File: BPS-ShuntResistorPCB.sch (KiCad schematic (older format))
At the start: 3 parts, among them J1 Conn_01x04

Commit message: fixed labels
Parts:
- J1: value Conn_01x04 -> Amp_Conn
- R1: value R -> 100u
- TH1: value Thermistor -> 100
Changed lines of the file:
@@
 P 6850 4350
 F 0 "J1" H 6950 4400 50  0000 L CNN
-F 1 "Conn_01x04" H 6950 4300 50  0000 L CNN
+F 1 "Amp_Conn" H 6950 4300 50  0000 L CNN
 F 2 "" H 6850 4350 50  0001 C CNN
 F 3 "~" H 6850 4350 50  0001 C CNN
@@
 P 5950 4150
 F 0 "R1" H 6020 4196 50  0000 L CNN
-F 1 "R" H 6020 4105 50  0000 L CNN
+F 1 "100u" H 6020 4105 50  0000 L CNN
 F 2 "Resistor_SMD:R_0805_2012Metric" V 5880 4150 50  0001 C CNN
 F 3 "~" H 5950 4150 50  0001 C CNN
@@
 P 5950 4650
 F 0 "TH1" H 6055 4696 50  0000 L CNN
-F 1 "Thermistor" H 6055 4605 50  0000 L CNN
+F 1 "100" H 6055 4605 50  0000 L CNN
 F 2 "Resistor_SMD:R_0805_2012Metric" H 5950 4650 50  0001 C CNN
 F 3 "~" H 5950 4650 50  0001 C CNN

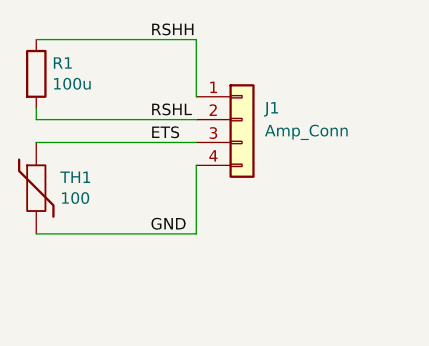
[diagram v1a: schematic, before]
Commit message: added logos and conn footprint
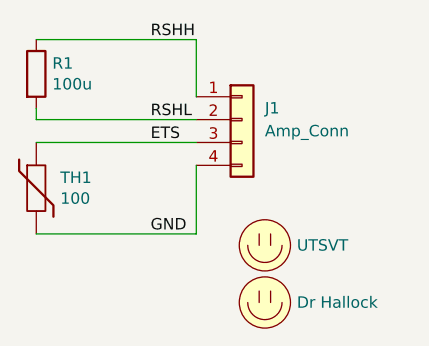
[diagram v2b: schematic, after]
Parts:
- added LOGO1: UTSVT, UTSVT_Special:UTSVT_Logo_Symbol, symbol utsvt-misc:Logo_Placeholder
- added LOGO2: Dr Hallock, UTSVT_Special:Hallock_Image_Tiny, symbol utsvt-misc:Logo_Placeholder
- J1: footprint (none) -> UTSVT_Connectors:Power_Metal_Strip_Battery_Shunt_Resistor_4_Pin_Connector
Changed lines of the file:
@@
 F 0 "J1" H 6950 4400 50  0000 L CNN
 F 1 "Amp_Conn" H 6950 4300 50  0000 L CNN
-F 2 "" H 6850 4350 50  0001 C CNN
+F 2 "UTSVT_Connectors:Power_Metal_Strip_Battery_Shunt_Resistor_4_Pin_Connector" H 6850 4350 50  0001 C CNN
 F 3 "~" H 6850 4350 50  0001 C CNN
 	1    6850 4350
@@
 	1    0    0    -1
 $EndComp
+$Comp
+L utsvt-misc:Logo_Placeholder LOGO1
+U 1 1 5F53FE42
+P 6950 4900
+F 0 "LOGO1" H 6950 5050 50  0001 C CNN
+F 1 "UTSVT" H 7090 4900 50  0000 L CNN
+F 2 "UTSVT_Special:UTSVT_Logo_Symbol" H 6950 4975 50  0001 C CNN
+F 3 "" H 6950 4975 50  0001 C CNN
+	1    6950 4900
+	1    0    0    -1
+$EndComp
+$Comp
+L utsvt-misc:Logo_Placeholder LOGO2
+U 1 1 5F5407D9
+P 6950 5150
+F 0 "LOGO2" H 6950 5300 50  0001 C CNN
+F 1 "Dr Hallock" H 7090 5150 50  0000 L CNN
+F 2 "UTSVT_Special:Hallock_Image_Tiny" H 6950 5225 50  0001 C CNN
+F 3 "" H 6950 5225 50  0001 C CNN
+	1    6950 5150
+	1    0    0    -1
+$EndComp

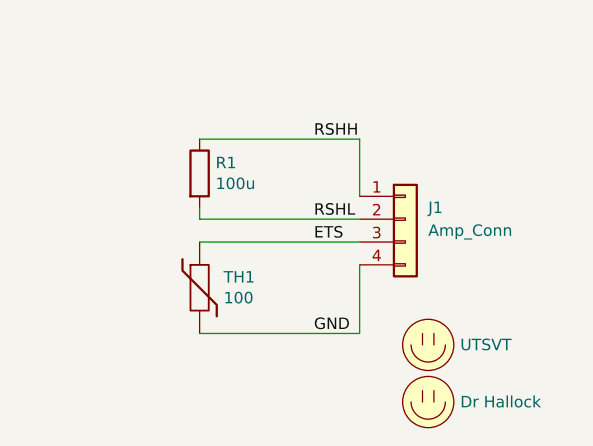
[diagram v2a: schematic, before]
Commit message: updated connector to match ampere board
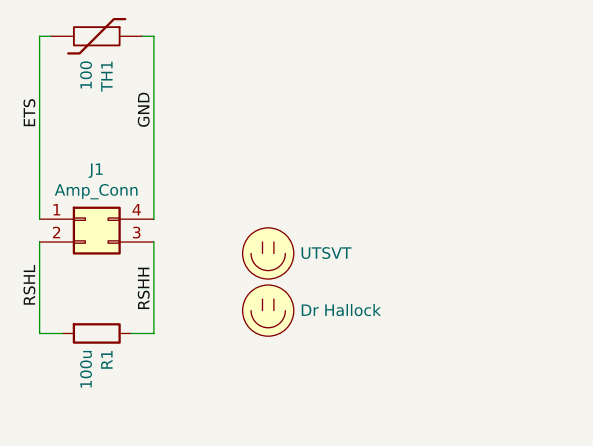
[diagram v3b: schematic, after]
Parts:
- removed J1: Amp_Conn, UTSVT_Connectors:Power_Metal_Strip_Battery_Shunt_Resistor_4_Pin_Connector, symbol Connector_Generic:Conn_01x04
- added J1: Amp_Conn, UTSVT_Connectors:Power_Metal_Strip_Battery_Shunt_Resistor_4_Pin_Connector, symbol Connector_Generic:Conn_02x02_Counter_Clockwise
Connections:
- net ETS: now also TH1.2, J1.1 (Pin_1); no longer TH1.1
- net GND: now also TH1.1, J1.4 (Pin_4); no longer TH1.2
- net RSHH: now also J1.3 (Pin_3)
- net RSHL: now also J1.2 (Pin_2)
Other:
- moved on the sheet: R1, TH1
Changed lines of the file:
@@
 Comment4 ""
 $EndDescr
-Wire Wire Line
-	6650 4250 6650 4000
-Wire Wire Line
-	6650 4000 5950 4000
-Wire Wire Line
-	5950 4300 5950 4350
-Wire Wire Line
-	5950 4350 6650 4350
-Wire Wire Line
-	6650 4550 6650 4850
-Wire Wire Line
-	6650 4850 5950 4850
-Wire Wire Line
-	5950 4450 6650 4450
-Text Label 6450 4000 0    50   ~ 0
+Text Label 5750 4750 1    50   ~ 0
 RSHH
-Text Label 6450 4350 0    50   ~ 0
+Text Label 5250 4550 3    50   ~ 0
 RSHL
-Text Label 6450 4450 0    50   ~ 0
+Text Label 5250 3950 1    50   ~ 0
 ETS
-Text Label 6450 4850 0    50   ~ 0
+Text Label 5750 3950 1    50   ~ 0
 GND
 $Comp
-L Connector_Generic:Conn_01x04 J1
-U 1 1 5F54708B
-P 6850 4350
-F 0 "J1" H 6950 4400 50  0000 L CNN
-F 1 "Amp_Conn" H 6950 4300 50  0000 L CNN
-F 2 "UTSVT_Connectors:Power_Metal_Strip_Battery_Shunt_Resistor_4_Pin_Connector" H 6850 4350 50  0001 C CNN
-F 3 "~" H 6850 4350 50  0001 C CNN
-	1    6850 4350
+L Device:Thermistor TH1
+U 1 1 5F548CAA
+P 5500 3550
+F 0 "TH1" H 5605 3596 50  0000 L CNN
+F 1 "100" H 5605 3505 50  0000 L CNN
+F 2 "Resistor_SMD:R_0805_2012Metric" H 5500 3550 50  0001 C CNN
+F 3 "~" H 5500 3550 50  0001 C CNN
+	1    5500 3550
+	0    1    1    0
+$EndComp
+$Comp
+L utsvt-misc:Logo_Placeholder LOGO1
+U 1 1 5F53FE42
+P 6250 4500
+F 0 "LOGO1" H 6250 4650 50  0001 C CNN
+F 1 "UTSVT" H 6390 4500 50  0000 L CNN
+F 2 "UTSVT_Special:UTSVT_Logo_Symbol" H 6250 4575 50  0001 C CNN
+F 3 "" H 6250 4575 50  0001 C CNN
+	1    6250 4500
+	1    0    0    -1
+$EndComp
+$Comp
+L utsvt-misc:Logo_Placeholder LOGO2
+U 1 1 5F5407D9
+P 6250 4750
+F 0 "LOGO2" H 6250 4900 50  0001 C CNN
+F 1 "Dr Hallock" H 6390 4750 50  0000 L CNN
+F 2 "UTSVT_Special:Hallock_Image_Tiny" H 6250 4825 50  0001 C CNN
+F 3 "" H 6250 4825 50  0001 C CNN
+	1    6250 4750
 	1    0    0    -1
 $EndComp
@@
 L Device:R R1
 U 1 1 5F548200
-P 5950 4150
-F 0 "R1" H 6020 4196 50  0000 L CNN
-F 1 "100u" H 6020 4105 50  0000 L CNN
-F 2 "Resistor_SMD:R_0805_2012Metric" V 5880 4150 50  0001 C CNN
-F 3 "~" H 5950 4150 50  0001 C CNN
-	1    5950 4150
+P 5500 4850
+F 0 "R1" H 5570 4896 50  0000 L CNN
+F 1 "100u" H 5570 4805 50  0000 L CNN
+F 2 "Resistor_SMD:R_0805_2012Metric" V 5430 4850 50  0001 C CNN
+F 3 "~" H 5500 4850 50  0001 C CNN
+	1    5500 4850
+	0    1    1    0
+$EndComp
+$Comp
+L Connector_Generic:Conn_02x02_Counter_Clockwise J1
+U 1 1 5F55AEC1
+P 5450 4350
+F 0 "J1" H 5500 4567 50  0000 C CNN
+F 1 "Amp_Conn" H 5500 4476 50  0000 C CNN
+F 2 "UTSVT_Connectors:Power_Metal_Strip_Battery_Shunt_Resistor_4_Pin_Connector" H 5450 4350 50  0001 C CNN
+F 3 "~" H 5450 4350 50  0001 C CNN
+	1    5450 4350
 	1    0    0    -1
 $EndComp
-$Comp
-L Device:Thermistor TH1
-U 1 1 5F548CAA
-P 5950 4650
-F 0 "TH1" H 6055 4696 50  0000 L CNN
-F 1 "100" H 6055 4605 50  0000 L CNN
-F 2 "Resistor_SMD:R_0805_2012Metric" H 5950 4650 50  0001 C CNN
-F 3 "~" H 5950 4650 50  0001 C CNN
-	1    5950 4650
-	1    0    0    -1
-$EndComp
-$Comp
-L utsvt-misc:Logo_Placeholder LOGO1
-U 1 1 5F53FE42
-P 6950 4900
-F 0 "LOGO1" H 6950 5050 50  0001 C CNN
-F 1 "UTSVT" H 7090 4900 50  0000 L CNN
-F 2 "UTSVT_Special:UTSVT_Logo_Symbol" H 6950 4975 50  0001 C CNN
-F 3 "" H 6950 4975 50  0001 C CNN
-	1    6950 4900
-	1    0    0    -1
-$EndComp
-$Comp
-L utsvt-misc:Logo_Placeholder LOGO2
-U 1 1 5F5407D9
-P 6950 5150
-F 0 "LOGO2" H 6950 5300 50  0001 C CNN
-F 1 "Dr Hallock" H 7090 5150 50  0000 L CNN
-F 2 "UTSVT_Special:Hallock_Image_Tiny" H 6950 5225 50  0001 C CNN
-F 3 "" H 6950 5225 50  0001 C CNN
-	1    6950 5150
-	1    0    0    -1
-$EndComp
+Wire Wire Line
+	5250 4350 5250 3550
+Wire Wire Line
+	5250 3550 5300 3550
+Wire Wire Line
+	5750 4350 5750 3550
+Wire Wire Line
+	5750 3550 5700 3550
+Wire Wire Line
+	5250 4450 5250 4850
+Wire Wire Line
+	5250 4850 5350 4850
+Wire Wire Line
+	5650 4850 5750 4850
+Wire Wire Line
+	5750 4850 5750 4450
 $EndSCHEMATC

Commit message: added resistor footprint
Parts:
- R1: footprint Resistor_SMD:R_0805_2012Metric -> UTSVT_Passive:Power_Metal_Strip_Battery_Shunt_Resistor
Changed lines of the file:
@@
 F 0 "R1" H 5570 4896 50  0000 L CNN
 F 1 "100u" H 5570 4805 50  0000 L CNN
-F 2 "Resistor_SMD:R_0805_2012Metric" V 5430 4850 50  0001 C CNN
+F 2 "UTSVT_Passive:Power_Metal_Strip_Battery_Shunt_Resistor" V 5430 4850 50  0001 C CNN
 F 3 "~" H 5500 4850 50  0001 C CNN
 	1    5500 4850

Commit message: needs to be reviewed
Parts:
- added H1, H2: MountingHole, MountingHole:MountingHole_2.7mm_M2.5, symbol Mechanical:MountingHole
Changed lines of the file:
@@
 Wire Wire Line
 	5750 4850 5750 4450
+$Comp
+L Mechanical:MountingHole H1
+U 1 1 5F6F5E19
+P 3000 2100
+F 0 "H1" H 3100 2146 50  0000 L CNN
+F 1 "MountingHole" H 3100 2055 50  0000 L CNN
+F 2 "MountingHole:MountingHole_2.7mm_M2.5" H 3000 2100 50  0001 C CNN
+F 3 "~" H 3000 2100 50  0001 C CNN
+	1    3000 2100
+	1    0    0    -1
+$EndComp
+$Comp
+L Mechanical:MountingHole H2
+U 1 1 5F6F8A03
+P 2950 2900
+F 0 "H2" H 3050 2946 50  0000 L CNN
+F 1 "MountingHole" H 3050 2855 50  0000 L CNN
+F 2 "MountingHole:MountingHole_2.7mm_M2.5" H 2950 2900 50  0001 C CNN
+F 3 "~" H 2950 2900 50  0001 C CNN
+	1    2950 2900
+	1    0    0    -1
+$EndComp
 $EndSCHEMATC

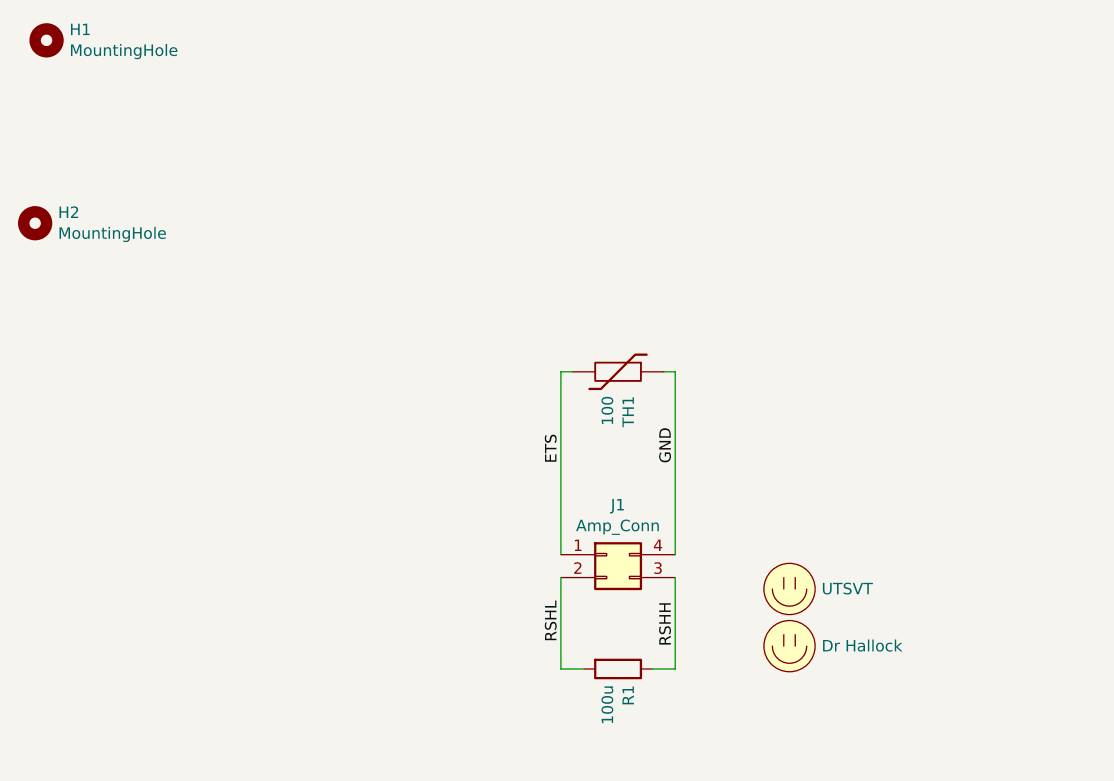
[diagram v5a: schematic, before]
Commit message: Organizes schematic and creates pdf and png files of schematic and PCB
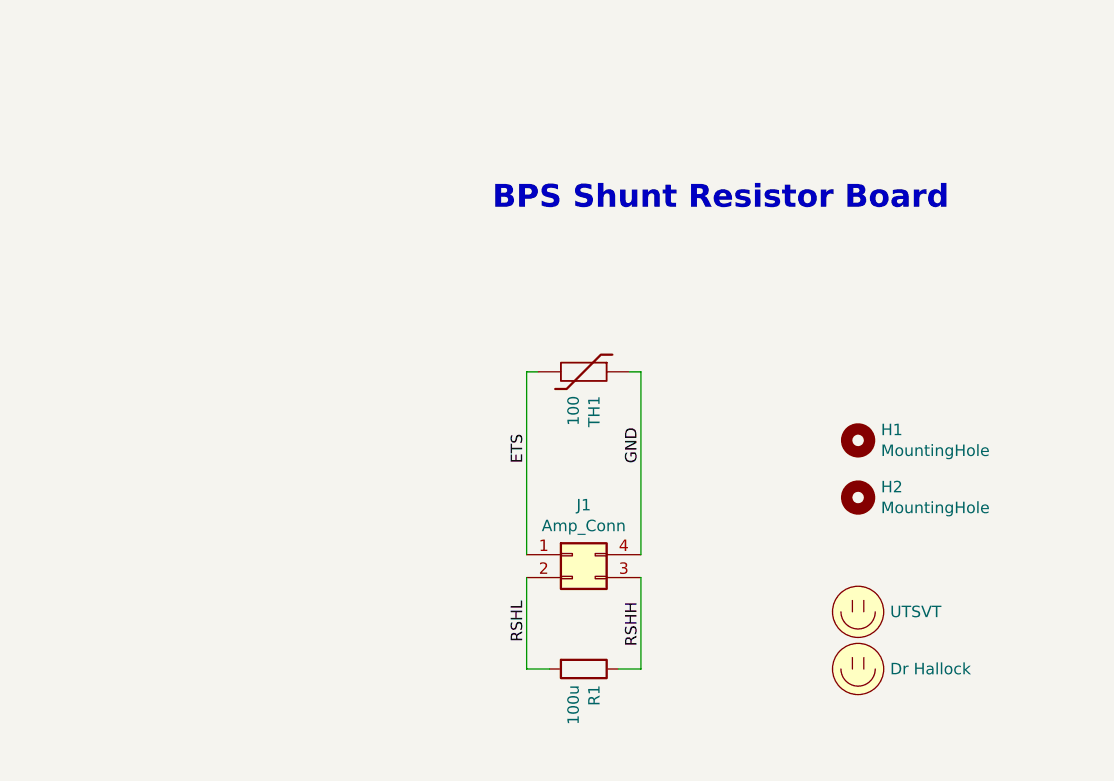
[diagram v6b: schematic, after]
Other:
- note added: "BPS Shunt Resistor Board"
- moved on the sheet: H1, H2, J1, R1, TH1
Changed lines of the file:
@@
 Comment4 ""
 $EndDescr
-Text Label 5750 4750 1    50   ~ 0
+Text Label 5600 4750 1    50   ~ 0
 RSHH
-Text Label 5250 4550 3    50   ~ 0
+Text Label 5100 4550 3    50   ~ 0
 RSHL
-Text Label 5250 3950 1    50   ~ 0
+Text Label 5100 3950 1    50   ~ 0
 ETS
-Text Label 5750 3950 1    50   ~ 0
+Text Label 5600 3950 1    50   ~ 0
 GND
 $Comp
 L Device:Thermistor TH1
 U 1 1 5F548CAA
-P 5500 3550
-F 0 "TH1" H 5605 3596 50  0000 L CNN
-F 1 "100" H 5605 3505 50  0000 L CNN
-F 2 "Resistor_SMD:R_0805_2012Metric" H 5500 3550 50  0001 C CNN
-F 3 "~" H 5500 3550 50  0001 C CNN
-	1    5500 3550
+P 5350 3550
+F 0 "TH1" H 5455 3596 50  0000 L CNN
+F 1 "100" H 5455 3505 50  0000 L CNN
+F 2 "Resistor_SMD:R_0805_2012Metric" H 5350 3550 50  0001 C CNN
+F 3 "~" H 5350 3550 50  0001 C CNN
+	1    5350 3550
 	0    1    1    0
 $EndComp
@@
 L utsvt-misc:Logo_Placeholder LOGO1
 U 1 1 5F53FE42
-P 6250 4500
-F 0 "LOGO1" H 6250 4650 50  0001 C CNN
-F 1 "UTSVT" H 6390 4500 50  0000 L CNN
-F 2 "UTSVT_Special:UTSVT_Logo_Symbol" H 6250 4575 50  0001 C CNN
-F 3 "" H 6250 4575 50  0001 C CNN
-	1    6250 4500
+P 6550 4600
+F 0 "LOGO1" H 6550 4750 50  0001 C CNN
+F 1 "UTSVT" H 6690 4600 50  0000 L CNN
+F 2 "UTSVT_Special:UTSVT_Logo_Symbol" H 6550 4675 50  0001 C CNN
+F 3 "" H 6550 4675 50  0001 C CNN
+	1    6550 4600
 	1    0    0    -1
 $EndComp
@@
 L utsvt-misc:Logo_Placeholder LOGO2
 U 1 1 5F5407D9
-P 6250 4750
-F 0 "LOGO2" H 6250 4900 50  0001 C CNN
-F 1 "Dr Hallock" H 6390 4750 50  0000 L CNN
-F 2 "UTSVT_Special:Hallock_Image_Tiny" H 6250 4825 50  0001 C CNN
-F 3 "" H 6250 4825 50  0001 C CNN
-	1    6250 4750
+P 6550 4850
+F 0 "LOGO2" H 6550 5000 50  0001 C CNN
+F 1 "Dr Hallock" H 6690 4850 50  0000 L CNN
+F 2 "UTSVT_Special:Hallock_Image_Tiny" H 6550 4925 50  0001 C CNN
+F 3 "" H 6550 4925 50  0001 C CNN
+	1    6550 4850
 	1    0    0    -1
 $EndComp
@@
 L Device:R R1
 U 1 1 5F548200
-P 5500 4850
-F 0 "R1" H 5570 4896 50  0000 L CNN
-F 1 "100u" H 5570 4805 50  0000 L CNN
-F 2 "UTSVT_Passive:Power_Metal_Strip_Battery_Shunt_Resistor" V 5430 4850 50  0001 C CNN
-F 3 "~" H 5500 4850 50  0001 C CNN
-	1    5500 4850
+P 5350 4850
+F 0 "R1" H 5420 4896 50  0000 L CNN
+F 1 "100u" H 5420 4805 50  0000 L CNN
+F 2 "UTSVT_Passive:Power_Metal_Strip_Battery_Shunt_Resistor" V 5280 4850 50  0001 C CNN
+F 3 "~" H 5350 4850 50  0001 C CNN
+	1    5350 4850
 	0    1    1    0
 $EndComp
@@
 L Connector_Generic:Conn_02x02_Counter_Clockwise J1
 U 1 1 5F55AEC1
-P 5450 4350
-F 0 "J1" H 5500 4567 50  0000 C CNN
-F 1 "Amp_Conn" H 5500 4476 50  0000 C CNN
-F 2 "UTSVT_Connectors:Power_Metal_Strip_Battery_Shunt_Resistor_4_Pin_Connector" H 5450 4350 50  0001 C CNN
-F 3 "~" H 5450 4350 50  0001 C CNN
-	1    5450 4350
+P 5300 4350
+F 0 "J1" H 5350 4567 50  0000 C CNN
+F 1 "Amp_Conn" H 5350 4476 50  0000 C CNN
+F 2 "UTSVT_Connectors:Power_Metal_Strip_Battery_Shunt_Resistor_4_Pin_Connector" H 5300 4350 50  0001 C CNN
+F 3 "~" H 5300 4350 50  0001 C CNN
+	1    5300 4350
 	1    0    0    -1
 $EndComp
 Wire Wire Line
-	5250 4350 5250 3550
+	5100 4350 5100 3550
 Wire Wire Line
-	5250 3550 5300 3550
+	5100 3550 5150 3550
 Wire Wire Line
-	5750 4350 5750 3550
+	5600 4350 5600 3550
 Wire Wire Line
-	5750 3550 5700 3550
+	5600 3550 5550 3550
 Wire Wire Line
-	5250 4450 5250 4850
+	5100 4450 5100 4850
 Wire Wire Line
-	5250 4850 5350 4850
+	5100 4850 5200 4850
 Wire Wire Line
-	5650 4850 5750 4850
+	5500 4850 5600 4850
 Wire Wire Line
-	5750 4850 5750 4450
+	5600 4850 5600 4450
 $Comp
 L Mechanical:MountingHole H1
 U 1 1 5F6F5E19
-P 3000 2100
-F 0 "H1" H 3100 2146 50  0000 L CNN
-F 1 "MountingHole" H 3100 2055 50  0000 L CNN
-F 2 "MountingHole:MountingHole_2.7mm_M2.5" H 3000 2100 50  0001 C CNN
-F 3 "~" H 3000 2100 50  0001 C CNN
-	1    3000 2100
+P 6550 3850
+F 0 "H1" H 6650 3896 50  0000 L CNN
+F 1 "MountingHole" H 6650 3805 50  0000 L CNN
+F 2 "MountingHole:MountingHole_2.7mm_M2.5" H 6550 3850 50  0001 C CNN
+F 3 "~" H 6550 3850 50  0001 C CNN
+	1    6550 3850
 	1    0    0    -1
 $EndComp
@@
 L Mechanical:MountingHole H2
 U 1 1 5F6F8A03
-P 2950 2900
-F 0 "H2" H 3050 2946 50  0000 L CNN
-F 1 "MountingHole" H 3050 2855 50  0000 L CNN
-F 2 "MountingHole:MountingHole_2.7mm_M2.5" H 2950 2900 50  0001 C CNN
-F 3 "~" H 2950 2900 50  0001 C CNN
-	1    2950 2900
+P 6550 4100
+F 0 "H2" H 6650 4146 50  0000 L CNN
+F 1 "MountingHole" H 6650 4055 50  0000 L CNN
+F 2 "MountingHole:MountingHole_2.7mm_M2.5" H 6550 4100 50  0001 C CNN
+F 3 "~" H 6550 4100 50  0001 C CNN
+	1    6550 4100
 	1    0    0    -1
 $EndComp
+Text Notes 4950 2850 0    100  ~ 20
+BPS Shunt Resistor Board
 $EndSCHEMATC
